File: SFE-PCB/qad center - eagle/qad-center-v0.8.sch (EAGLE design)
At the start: 81 parts, among them U1 LM75BGD, U2 AD5647R, U3 PCA9537, U4 LM75BGD, U5 LM96080

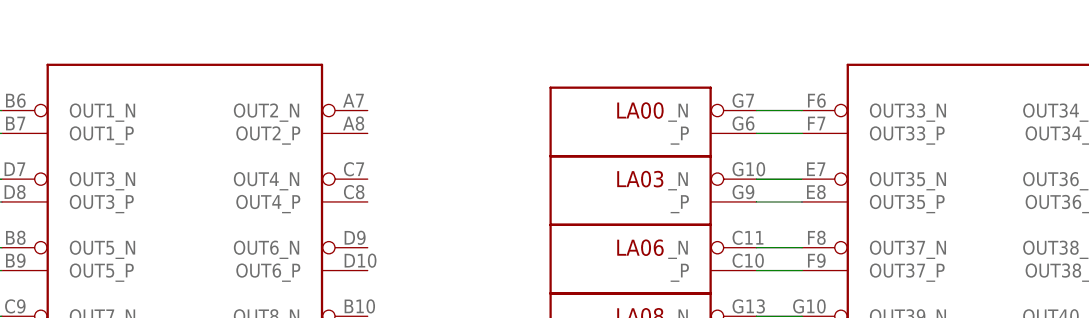
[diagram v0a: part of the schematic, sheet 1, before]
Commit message: added cmv12000 operation mode note
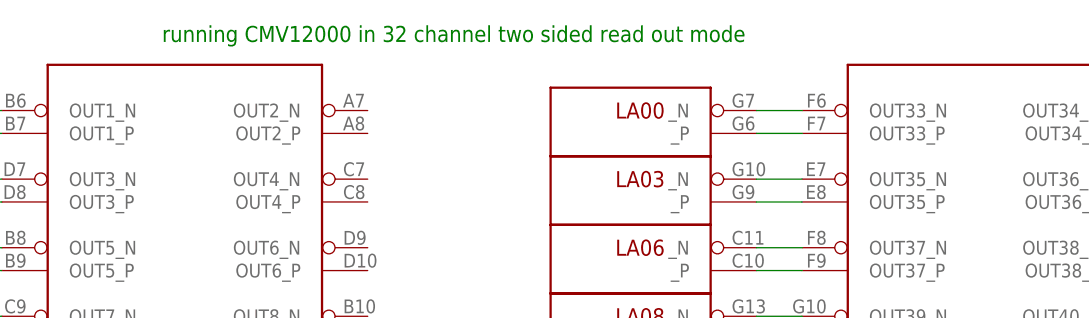
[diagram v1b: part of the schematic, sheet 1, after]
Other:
- note added: "running CMV12000 in 32 channel two sided read out mode"
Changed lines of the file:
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@@
 <?xml version="1.0" encoding="utf-8"?>
 <!DOCTYPE eagle SYSTEM "eagle.dtd">
-<eagle version="6.4.4">
+<eagle version="6.4">
 <drawing>
 <settings>
@@
 <setting verticaltext="up"/>
 </settings>
-<grid distance="0.1" unitdist="inch" unit="inch" style="lines" multiple="1" display="yes" altdistance="0.01" altunitdist="inch" altunit="inch"/>
+<grid distance="0.1" unitdist="inch" unit="inch" style="lines" multiple="1" display="no" altdistance="0.01" altunitdist="inch" altunit="inch"/>
 <layers>
-<layer number="1" name="Top" color="16" fill="1" visible="yes" active="no"/>
-<layer number="2" name="Route2" color="17" fill="1" visible="yes" active="no"/>
-<layer number="3" name="Route3" color="4" fill="3" visible="yes" active="no"/>
-<layer number="4" name="Route4" color="1" fill="4" visible="yes" active="no"/>
-<layer number="5" name="Route5" color="4" fill="4" visible="yes" active="no"/>
-<layer number="6" name="Route6" color="1" fill="8" visible="yes" active="no"/>
-<layer number="7" name="Route7" color="4" fill="8" visible="yes" active="no"/>
-<layer number="8" name="Route8" color="1" fill="2" visible="yes" active="no"/>
-<layer number="9" name="Route9" color="4" fill="2" visible="yes" active="no"/>
-<layer number="10" name="Route10" color="1" fill="7" visible="yes" active="no"/>
-<layer number="11" name="Route11" color="4" fill="7" visible="yes" active="no"/>
-<layer number="12" name="Route12" color="1" fill="5" visible="yes" active="no"/>
-<layer number="13" name="Route13" color="4" fill="5" visible="yes" active="no"/>
-<layer number="14" name="Route14" color="1" fill="6" visible="yes" active="no"/>
-<layer number="15" name="Route15" color="18" fill="1" visible="yes" active="no"/>
-<layer number="16" name="Bottom" color="19" fill="1" visible="yes" active="no"/>
-<layer number="17" name="Pads" color="2" fill="1" visible="yes" active="no"/>
-<layer number="18" name="Vias" color="2" fill="1" visible="yes" active="no"/>
-<layer number="19" name="Unrouted" color="6" fill="1" visible="yes" active="no"/>
-<layer number="20" name="Dimension" color="15" fill="1" visible="yes" active="no"/>
-<layer number="21" name="tPlace" color="7" fill="1" visible="yes" active="no"/>
-<layer number="22" name="bPlace" color="7" fill="1" visible="yes" active="no"/>
-<layer number="23" name="tOrigins" color="15" fill="1" visible="yes" active="no"/>
-<layer number="24" name="bOrigins" color="15" fill="1" visible="yes" active="no"/>
-<layer number="25" name="tNames" color="7" fill="1" visible="yes" active="no"/>
-<layer number="26" name="bNames" color="7" fill="1" visible="yes" active="no"/>
-<layer number="27" name="tValues" color="7" fill="1" visible="yes" active="no"/>
-<layer number="28" name="bValues" color="7" fill="1" visible="yes" active="no"/>
+<layer number="1" name="Top" color="16" fill="1" visible="no" active="no"/>
+<layer number="2" name="Route2" color="17" fill="1" visible="no" active="no"/>
+<layer number="3" name="Route3" color="4" fill="3" visible="no" active="no"/>
+<layer number="4" name="Route4" color="1" fill="4" visible="no" active="no"/>
+<layer number="5" name="Route5" color="4" fill="4" visible="no" active="no"/>
+<layer number="6" name="Route6" color="1" fill="8" visible="no" active="no"/>
+<layer number="7" name="Route7" color="4" fill="8" visible="no" active="no"/>
+<layer number="8" name="Route8" color="1" fill="2" visible="no" active="no"/>
+<layer number="9" name="Route9" color="4" fill="2" visible="no" active="no"/>
+<layer number="10" name="Route10" color="1" fill="7" visible="no" active="no"/>
+<layer number="11" name="Route11" color="4" fill="7" visible="no" active="no"/>
+<layer number="12" name="Route12" color="1" fill="5" visible="no" active="no"/>
+<layer number="13" name="Route13" color="4" fill="5" visible="no" active="no"/>
+<layer number="14" name="Route14" color="1" fill="6" visible="no" active="no"/>
+<layer number="15" name="Route15" color="18" fill="1" visible="no" active="no"/>
+<layer number="16" name="Bottom" color="19" fill="1" visible="no" active="no"/>
+<layer number="17" name="Pads" color="2" fill="1" visible="no" active="no"/>
+<layer number="18" name="Vias" color="2" fill="1" visible="no" active="no"/>
+<layer number="19" name="Unrouted" color="6" fill="1" visible="no" active="no"/>
+<layer number="20" name="Dimension" color="15" fill="1" visible="no" active="no"/>
+<layer number="21" name="tPlace" color="7" fill="1" visible="no" active="no"/>
+<layer number="22" name="bPlace" color="7" fill="1" visible="no" active="no"/>
+<layer number="23" name="tOrigins" color="15" fill="1" visible="no" active="no"/>
+<layer number="24" name="bOrigins" color="15" fill="1" visible="no" active="no"/>
+<layer number="25" name="tNames" color="7" fill="1" visible="no" active="no"/>
+<layer number="26" name="bNames" color="7" fill="1" visible="no" active="no"/>
+<layer number="27" name="tValues" color="7" fill="1" visible="no" active="no"/>
+<layer number="28" name="bValues" color="7" fill="1" visible="no" active="no"/>
 <layer number="29" name="tStop" color="7" fill="3" visible="no" active="no"/>
 <layer number="30" name="bStop" color="7" fill="6" visible="no" active="no"/>
@@
 <layer number="35" name="tGlue" color="7" fill="4" visible="no" active="no"/>
 <layer number="36" name="bGlue" color="7" fill="5" visible="no" active="no"/>
-<layer number="37" name="tTest" color="7" fill="1" visible="yes" active="no"/>
-<layer number="38" name="bTest" color="7" fill="1" visible="yes" active="no"/>
+<layer number="37" name="tTest" color="7" fill="1" visible="no" active="no"/>
+<layer number="38" name="bTest" color="7" fill="1" visible="no" active="no"/>
 <layer number="39" name="tKeepout" color="4" fill="11" visible="no" active="no"/>
 <layer number="40" name="bKeepout" color="1" fill="11" visible="no" active="no"/>
@@
 <layer number="44" name="Drills" color="7" fill="1" visible="no" active="no"/>
 <layer number="45" name="Holes" color="7" fill="1" visible="no" active="no"/>
-<layer number="46" name="Milling" color="3" fill="1" visible="yes" active="no"/>
-<layer number="47" name="Measures" color="7" fill="1" visible="yes" active="no"/>
-<layer number="48" name="Document" color="7" fill="1" visible="yes" active="no"/>
-<layer number="49" name="Reference" color="7" fill="1" visible="yes" active="no"/>
-<layer number="50" name="dxf" color="7" fill="1" visible="yes" active="no"/>
-<layer number="51" name="tDocu" color="7" fill="1" visible="yes" active="no"/>
-<layer number="52" name="bDocu" color="7" fill="1" visible="yes" active="no"/>
-<layer number="53" name="tGND_GNDA" color="7" fill="9" visible="yes" active="no"/>
-<layer number="54" name="bGND_GNDA" color="1" fill="9" visible="yes" active="no"/>
-<layer number="56" name="wert" color="7" fill="1" visible="yes" active="no"/>
+<layer number="46" name="Milling" color="3" fill="1" visible="no" active="no"/>
+<layer number="47" name="Measures" color="7" fill="1" visible="no" active="no"/>
+<layer number="48" name="Document" color="7" fill="1" visible="no" active="no"/>
+<layer number="49" name="Reference" color="7" fill="1" visible="no" active="no"/>
+<layer number="50" name="dxf" color="7" fill="1" visible="no" active="no"/>
+<layer number="51" name="tDocu" color="7" fill="1" visible="no" active="no"/>
+<layer number="52" name="bDocu" color="7" fill="1" visible="no" active="no"/>
+<layer number="53" name="tGND_GNDA" color="7" fill="9" visible="no" active="no"/>
+<layer number="54" name="bGND_GNDA" color="1" fill="9" visible="no" active="no"/>
+<layer number="56" name="wert" color="7" fill="1" visible="no" active="no"/>
 <layer number="91" name="Nets" color="2" fill="1" visible="yes" active="yes"/>
 <layer number="92" name="Busses" color="1" fill="1" visible="yes" active="yes"/>
@@
 <text x="381" y="20.32" size="2.54" layer="97" align="bottom-right">&gt;VERSION</text>
 <text x="289.56" y="17.78" size="2.54" layer="94" align="top-left">LVDS and Control Interface</text>
+<text x="218.44" y="205.74" size="1.778" layer="91">running CMV12000 in 32 channel two sided read out mode</text>
 </plain>
 <instances>
